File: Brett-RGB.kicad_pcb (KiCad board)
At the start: 2 copper layers, 223 x 71 mm, 182 parts, among them P1 CONN_02X05, P2 USB_OTG, SW1 SW_PUSH, SW10 SW_PUSH, SW11 SW_PUSH, SW12 SW_PUSH, SW13 SW_PUSH, SW14 SW_PUSH, SW15 SW_PUSH, SW16 SW_PUSH, SW17 SW_PUSH, SW18 SW_PUSH, SW19 SW_PUSH, SW2 SW_PUSH, SW20 SW_PUSH, SW21 SW_PUSH, SW22 SW_PUSH, SW23 SW_PUSH, SW24 SW_PUSH, SW25 SW_PUSH, SW26 SW_PUSH, SW27 SW_PUSH, SW28 SW_PUSH, SW29 SW_PUSH, SW3 SW_PUSH, SW30 SW_PUSH, SW31 SW_PUSH, SW32 SW_PUSH, SW33 SW_PUSH, SW34 SW_PUSH, SW35 SW_PUSH, SW36 SW_PUSH, SW37 SW_PUSH, SW38 SW_PUSH, SW39 SW_PUSH, SW4 SW_PUSH, SW40 SW_PUSH, SW41 SW_PUSH, SW42 SW_PUSH, SW43 SW_PUSH, SW44 SW_PUSH, SW45 SW_PUSH, SW46 SW_PUSH, SW47 SW_PUSH, SW48 Reset, SW5 SW_PUSH, SW6 SW_PUSH, SW7 SW_PUSH, SW8 SW_PUSH, SW9 SW_PUSH, U1 IS31FL3732, U2 MK20DX256VLH7, X1 CRYSTAL_SMD

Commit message: Reworked the Board
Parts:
- removed C14, C15, C17, C20, C21: 0.1uF, Capacitors_SMD:C_0603
- removed C18, C19: 1uF, Capacitors_SMD:C_0603
- removed D48: LED, LEDs:LED_0805
- removed D49, D50, D51, D52, D53, D54, D55, D56, D57, D58, D59, D60, D61, D62, D63, D64, D65, D66, D67, D68, D69, D70, D71, D72, D73, D74, D75, D76, D77, D78, D79, D80, D81, D82, D83, D84, D85, D86, D87, D88, D89, D90, D91, D92, D93, D94, D95: D_Small, Diodes_SMD:SOD-123
- added C11: 0.1uF, Capacitors_SMD:C_0603, B.Cu at (97.2, 64.8)
- added LED1: Led_RGB_CA, lib.pretty:RGB-0606, F.Cu at (45.0, 42.0)
- added LED10: Led_RGB_CA, lib.pretty:RGB-0606, F.Cu at (216.0, 42.0)
- added LED11: Led_RGB_CA, lib.pretty:RGB-0606, F.Cu at (235.0, 42.0)
- added LED12: Led_RGB_CA, lib.pretty:RGB-0606, F.Cu at (254.0, 42.0)
- added LED13: Led_RGB_CA, lib.pretty:RGB-0606, F.Cu at (45.0, 61.0)
- added LED14: Led_RGB_CA, lib.pretty:RGB-0606, F.Cu at (64.0, 61.0)
- added LED15: Led_RGB_CA, lib.pretty:RGB-0606, F.Cu at (83.0, 61.0)
- added LED16: Led_RGB_CA, lib.pretty:RGB-0606, F.Cu at (102.0, 61.0)
- added LED17: Led_RGB_CA, lib.pretty:RGB-0606, F.Cu at (121.0, 61.0)
- added LED18: Led_RGB_CA, lib.pretty:RGB-0606, F.Cu at (140.0, 61.0)
- added LED19: Led_RGB_CA, lib.pretty:RGB-0606, F.Cu at (159.0, 61.0)
- added LED2: Led_RGB_CA, lib.pretty:RGB-0606, F.Cu at (64.0, 42.0)
- added LED20: Led_RGB_CA, lib.pretty:RGB-0606, F.Cu at (178.0, 61.0)
- added LED21: Led_RGB_CA, lib.pretty:RGB-0606, F.Cu at (197.0, 61.0)
- added LED22: Led_RGB_CA, lib.pretty:RGB-0606, F.Cu at (216.0, 61.0)
- added LED23: Led_RGB_CA, lib.pretty:RGB-0606, F.Cu at (235.0, 61.0)
- added LED24: Led_RGB_CA, lib.pretty:RGB-0606, F.Cu at (254.0, 61.0)
- added LED25: Led_RGB_CA, lib.pretty:RGB-0606, F.Cu at (45.0, 80.0)
- added LED26: Led_RGB_CA, lib.pretty:RGB-0606, F.Cu at (64.0, 80.0)
- added LED27: Led_RGB_CA, lib.pretty:RGB-0606, F.Cu at (83.0, 80.0)
- added LED28: Led_RGB_CA, lib.pretty:RGB-0606, F.Cu at (102.0, 80.0)
- added LED29: Led_RGB_CA, lib.pretty:RGB-0606, F.Cu at (121.0, 80.0)
- added LED3: Led_RGB_CA, lib.pretty:RGB-0606, F.Cu at (83.0, 42.0)
- added LED30: Led_RGB_CA, lib.pretty:RGB-0606, F.Cu at (140.0, 80.0)
- added LED31: Led_RGB_CA, lib.pretty:RGB-0606, F.Cu at (159.0, 80.0)
- added LED32: Led_RGB_CA, lib.pretty:RGB-0606, F.Cu at (178.0, 80.0)
- added LED33: Led_RGB_CA, lib.pretty:RGB-0606, F.Cu at (197.0, 80.0)
- added LED34: Led_RGB_CA, lib.pretty:RGB-0606, F.Cu at (216.0, 80.0)
- added LED35: Led_RGB_CA, lib.pretty:RGB-0606, F.Cu at (235.0, 80.0)
- added LED36: Led_RGB_CA, lib.pretty:RGB-0606, F.Cu at (254.0, 80.0)
- added LED37: Led_RGB_CA, lib.pretty:RGB-0606, F.Cu at (45.0, 99.0)
- added LED38: Led_RGB_CA, lib.pretty:RGB-0606, F.Cu at (64.0, 99.0)
- added LED39: Led_RGB_CA, lib.pretty:RGB-0606, F.Cu at (83.0, 99.0)
- added LED4: Led_RGB_CA, lib.pretty:RGB-0606, F.Cu at (102.0, 42.0)
- added LED40: Led_RGB_CA, lib.pretty:RGB-0606, F.Cu at (102.0, 99.0)
- added LED41: Led_RGB_CA, lib.pretty:RGB-0606, F.Cu at (121.0, 99.0)
- added LED42: Led_RGB_CA, lib.pretty:RGB-0606, F.Cu at (149.5, 99.0)
- added LED43: Led_RGB_CA, lib.pretty:RGB-0606, F.Cu at (178.0, 99.0)
- added LED44: Led_RGB_CA, lib.pretty:RGB-0606, F.Cu at (197.0, 99.0)
- added LED45: Led_RGB_CA, lib.pretty:RGB-0606, F.Cu at (216.0, 99.0)
- added LED46: Led_RGB_CA, lib.pretty:RGB-0606, F.Cu at (235.0, 99.0)
- added LED47: Led_RGB_CA, lib.pretty:RGB-0606, F.Cu at (254.0, 99.0)
- added LED48: LED, lib.pretty:LED_0805, B.Cu at (87.5, 44.0)
- added LED5: Led_RGB_CA, lib.pretty:RGB-0606, F.Cu at (121.0, 42.0)
- added LED6: Led_RGB_CA, lib.pretty:RGB-0606, F.Cu at (140.0, 42.0)
- added LED7: Led_RGB_CA, lib.pretty:RGB-0606, F.Cu at (159.0, 42.0)
- added LED8: Led_RGB_CA, lib.pretty:RGB-0606, F.Cu at (178.0, 42.0)
- added LED9: Led_RGB_CA, lib.pretty:RGB-0606, F.Cu at (197.0, 42.0)
- added P3: CONN_01X04, lib.pretty:Conn-4, B.Cu at (97.0, 57.0)
- added P4: FLASH_HDR, lib.pretty:JLINK_NEEDLE, B.Cu at (95.0, 51.0)
- added P5: CONN_01X04, lib.pretty:Conn-4, B.Cu at (106.5, 68.8)
- added P6: CONN_01X02, lib.pretty:Conn-2, B.Cu at (92.5, 85.8)
- added P7: CONN_01X02, lib.pretty:Conn-2, B.Cu at (80.5, 75.0)
- added R11: 100, Resistors_SMD:R_0603, B.Cu at (100.0, 59.5)
- C1: value 100uF -> 0.1uF; footprint Capacitors_SMD:C_0805 -> Capacitors_SMD:C_0603
- C12: value 100n -> 0.1uF
- C13, C3: value 1uF -> 0.1uF
- C4: value 0.1uF -> 100uF; footprint Capacitors_SMD:C_0603 -> Capacitors_SMD:C_1206
- C5, C7: value 0.1uF -> 1uF
- C9: value 2.2uF -> 0.1uF
- D1, D10, D11, D12, D13, D14, D15, D16, D17, D18, D19, D2, D20, D21, D22, D23, D24, D25, D26, D27, D28, D29, D3, D30, D31, D32, D33, D34, D35, D36, D37, D38, D39, D4, D40, D41, D42, D43, D44, D45, D46, D47, D5, D6, D7, D8, D9: value LED_RGB -> D_Small; footprint mx2a:plcc-6 -> lib.pretty:SOD-123
- P1: value CONN_02X05 -> USB_OTG; footprint Pin_Headers:Pin_Header_Straight_2x05 -> lib.pretty:Micro-USB_629105150521
- P2: value USB_OTG -> CONN_01X04; footprint Connect:USB_Micro-B -> lib.pretty:Conn-4
- R1: value 1k -> 100k; moved to F.Cu
- R2: moved to F.Cu
- R3: value 33 -> 4.7k; moved to F.Cu
- R4: value 33 -> 100k
- R5: value 5M -> 4.7k; footprint Resistors_SMD:R_0805 -> Resistors_SMD:R_0603; moved to F.Cu
- R6: value 20k -> 33
- R7: value 1k -> 33
- R8: value 1k -> 20k
- R9: value 100k -> 5M; footprint Resistors_SMD:R_0603 -> Resistors_SMD:R_0805
- SW1, SW10, SW11, SW12, SW13, SW14, SW15, SW16, SW17, SW18, SW19, SW2, SW20, SW21, SW22, SW23, SW24, SW25, SW26, SW27, SW28, SW29, SW3, SW30, SW31, SW32, SW33, SW34, SW35, SW36, SW37, SW38, SW39, SW4, SW40, SW41, SW42, SW43, SW44, SW45, SW46, SW47, SW5, SW6, SW7, SW8, SW9: footprint mx2a:RomerG -> lib.pretty:RomerG
- SW48: value Reset -> TAC_SWITCH; footprint mx2a:KSEM31GLFS -> lib.pretty:PTS810
- U1: value IS31FL3732 -> IS31FL3737
- U2: value MK20DX256VLH7 -> MK20DX256VLH7-RESCUE-RainbowFox
- moved C4 66.4 mm to (73.5, 43.5)
- moved R4 50.7 mm to (115.8, 72.0), turned to 180 degrees
- moved R6 42.3 mm to (81.5, 70.0), turned to 180 degrees
- moved R3 42.1 mm to (103.5, 71.2), turned to 90 degrees
- moved P1 39.9 mm to (73.5, 32.0), turned to 0 degrees
- moved R7 39.3 mm to (81.5, 72.0), turned to 180 degrees
- moved R9 38.9 mm to (84.5, 68.2)
- moved P2 34.8 mm to (78.0, 72.0), turned to 90 degrees
- moved R1 28.1 mm to (107.5, 71.2)
- moved C5 28.0 mm to (107.2, 72.8), turned to 90 degrees
- moved C3 26.5 mm to (108.8, 72.8), turned to 90 degrees
- moved C13 25.1 mm to (102.0, 72.8), turned to 0 degrees
- moved C2 24.4 mm to (111.0, 72.2), turned to 180 degrees
- moved C12 22.2 mm to (92.5, 39.5), turned to 90 degrees
- moved C1 20.1 mm to (111.0, 70.8), turned to 180 degrees
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- renumbered REF** to ?
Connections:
- net /MCU/X+ renamed Net-(U2-Pad32)
- net /MCU/X- renamed Net-(U2-Pad33)
- C1 pad 1: GND -> +3V3
- C1 pad 2: +5V -> GND
- C10 pad 1: GND -> +5V
- C10 pad 2: +5V -> GND
- C13 pad 1: +5V -> +3V3
- C2 pad 1: +5V -> +3V3
- C6 pad 1: +3V3 -> +5V
- C7 pad 1: +3V3 -> +5V
- C8 pad 2: GND -> Net-(C8-Pad2)
- C9 pad 1: Net-(C9-Pad1) -> +3V3
- C9 pad 2: +3V3 -> GND
- D1 pad 1: /MCU/A1 -> /MCU/PTD0
- D1 pad 2: /MCU/A2 -> Net-(D1-Pad2)
- D10 pad 1: /MCU/A9 -> /MCU/PTC9
- D10 pad 2: /MCU/A9 -> Net-(D10-Pad2)
- D11 pad 1: /MCU/A7 -> /MCU/PTC9
- D11 pad 2: /MCU/A7 -> Net-(D11-Pad2)
- D12 pad 1: /MCU/A7 -> /MCU/PTC9
- D12 pad 2: /MCU/A8 -> Net-(D12-Pad2)
- D13 pad 1: /MCU/A5 -> /MCU/PTD1
- D13 pad 2: /MCU/A5 -> Net-(D13-Pad2)
- D14 pad 1: /MCU/A4 -> /MCU/PTD1
- D14 pad 2: /MCU/A4 -> Net-(D14-Pad2)
- D15 pad 1: /MCU/A3 -> /MCU/PTD1
- D15 pad 2: /MCU/A2 -> Net-(D15-Pad2)
- D16 pad 1: /MCU/A2 -> /MCU/PTD1
- D16 pad 2: /MCU/A3 -> Net-(D16-Pad2)
- D17 pad 1: /MCU/A1 -> /MCU/PTD1
- D17 pad 2: /MCU/A1 -> Net-(D17-Pad2)
- D18 pad 1: /MCU/A6 -> /MCU/PTD1
- D18 pad 2: /MCU/A6 -> Net-(D18-Pad2)
- D19 pad 1: /MCU/A5 -> /MCU/PTC8
- D19 pad 2: /MCU/A4 -> Net-(D19-Pad2)
- D2 pad 1: /MCU/A3 -> /MCU/PTD0
- D2 pad 2: /MCU/A2 -> Net-(D2-Pad2)
- D20 pad 1: /MCU/A4 -> /MCU/PTC8
- D20 pad 2: /MCU/A4 -> Net-(D20-Pad2)
- D21 pad 1: /MCU/A7 -> /MCU/PTC8
- D21 pad 2: /MCU/A8 -> Net-(D21-Pad2)
- D22 pad 1: /MCU/A5 -> /MCU/PTC8
- D22 pad 2: /MCU/A5 -> Net-(D22-Pad2)
- D23 pad 1: /MCU/A7 -> /MCU/PTC8
- D23 pad 2: /MCU/A8 -> Net-(D23-Pad2)
- D24 pad 1: /MCU/A6 -> /MCU/PTC8
- D24 pad 2: /MCU/A6 -> Net-(D24-Pad2)
- D25 pad 1: /MCU/B7 -> /MCU/PTD4
- D25 pad 2: /MCU/B8 -> Net-(D25-Pad2)
- D26 pad 1: /MCU/B7 -> /MCU/PTD4
- D26 pad 2: /MCU/B8 -> Net-(D26-Pad2)
- D27 pad 1: /MCU/B4 -> /MCU/PTD4
- D27 pad 2: /MCU/B4 -> Net-(D27-Pad2)
- D28 pad 1: /MCU/B5 -> /MCU/PTD4
- D28 pad 2: /MCU/B6 -> Net-(D28-Pad2)
- D29 pad 1: /MCU/B4 -> /MCU/PTD4
- D29 pad 2: /MCU/B4 -> Net-(D29-Pad2)
- D3 pad 1: /MCU/A6 -> /MCU/PTD0
- D3 pad 2: /MCU/A6 -> Net-(D3-Pad2)
- D30 pad 1: /MCU/B3 -> /MCU/PTD4
- D30 pad 2: /MCU/B3 -> Net-(D30-Pad2)
- D31 pad 1: /MCU/B2 -> /MCU/PTC7
- D31 pad 2: /MCU/B1 -> Net-(D31-Pad2)
- D32 pad 1: /MCU/B1 -> /MCU/PTC7
- D32 pad 2: /MCU/B2 -> Net-(D32-Pad2)
- D33 pad 1: /MCU/B4 -> /MCU/PTC7
- D33 pad 2: /MCU/B4 -> Net-(D33-Pad2)
- D34 pad 1: /MCU/B1 -> /MCU/PTC7
- D34 pad 2: /MCU/B2 -> Net-(D34-Pad2)
- D35 pad 1: /MCU/B5 -> /MCU/PTC7
- D35 pad 2: /MCU/B5 -> Net-(D35-Pad2)
- D36 pad 1: /MCU/B1 -> /MCU/PTC7
- D36 pad 2: /MCU/B2 -> Net-(D36-Pad2)
- D37 pad 1: /MCU/B5 -> /MCU/PTC11
- D37 pad 2: /MCU/B5 -> Net-(D37-Pad2)
- D38 pad 1: /MCU/B9 -> /MCU/PTC11
- D38 pad 2: /MCU/B9 -> Net-(D38-Pad2)
- D39 pad 1: /MCU/B8 -> /MCU/PTC11
- D39 pad 2: /MCU/B7 -> Net-(D39-Pad2)
- D4 pad 1: /MCU/A3 -> /MCU/PTD0
- D4 pad 2: /MCU/A2 -> Net-(D4-Pad2)
- D40 pad 1: /MCU/B6 -> /MCU/PTC11
- D40 pad 2: /MCU/B6 -> Net-(D40-Pad2)
- D41 pad 1: /MCU/B9 -> /MCU/PTC11
- D41 pad 2: /MCU/B8 -> Net-(D41-Pad2)
- D42 pad 1: /MCU/B9 -> /MCU/PTC11
- D42 pad 2: /MCU/B9 -> Net-(D42-Pad2)
- D43 pad 1: /MCU/B3 -> /MCU/PTC10
- D43 pad 2: /MCU/B2 -> Net-(D43-Pad2)
- D44 pad 1: /MCU/B1 -> /MCU/PTC10
- D44 pad 2: /MCU/B2 -> Net-(D44-Pad2)
- D45 pad 1: /MCU/B7 -> /MCU/PTC10
- D45 pad 2: /MCU/B7 -> Net-(D45-Pad2)
- D46 pad 1: /MCU/B1 -> /MCU/PTC10
- D46 pad 2: /MCU/B2 -> Net-(D46-Pad2)
- D47 pad 1: /MCU/B6 -> /MCU/PTC10
- D47 pad 2: /MCU/B6 -> Net-(D47-Pad2)
- D5 pad 1: /MCU/A7 -> /MCU/PTD0
- D5 pad 2: /MCU/A7 -> Net-(D5-Pad2)
- D6 pad 1: /MCU/A3 -> /MCU/PTD0
- D6 pad 2: /MCU/A2 -> Net-(D6-Pad2)
- D7 pad 1: /MCU/A8 -> /MCU/PTC9
- D7 pad 2: /MCU/A8 -> Net-(D7-Pad2)
- D8 pad 1: /MCU/A3 -> /MCU/PTC9
- D8 pad 2: /MCU/A2 -> Net-(D8-Pad2)
- D9 pad 1: /MCU/A9 -> /MCU/PTC9
- D9 pad 2: /MCU/A9 -> Net-(D9-Pad2)
- P1 pad 1: GND -> +5V
- P1 pad 2: (no net) -> /MCU/USB_D-
- P1 pad 3: +5V -> /MCU/USB_D+
- P1 pad 5: (no net) -> GND
- P2 pad 2: Net-(P2-Pad2) -> /MCU/USB_D-
- P2 pad 3: Net-(P2-Pad3) -> /MCU/USB_D+
- P2 pad 4: (no net) -> GND
- R1 pad 1: Net-(D48-Pad1) -> GND
- R1 pad 2: GND -> /MCU/SDB
- R10 pad 1: /MCU/SWD_CLK -> Net-(R10-Pad1)
- R10 pad 2: Net-(R10-Pad2) -> /MCU/SWD_CLK
- R2 pad 1: /MCU/INTB -> +3V3
- R2 pad 2: Net-(R2-Pad2) -> /MCU/INTB
- R3 pad 1: Net-(P2-Pad2) -> +3V3
- R3 pad 2: /MCU/D- -> /MCU/SCL
- R4 pad 1: Net-(P2-Pad3) -> GND
- R4 pad 2: /MCU/D+ -> Net-(R4-Pad2)
- R5 pad 1: Net-(C9-Pad1) -> +3V3
- R5 pad 2: GND -> /MCU/SDA
- R6 pad 1: GND -> /MCU/D-
- R6 pad 2: /MCU/R_Ext -> /MCU/USB_D-
- R7 pad 1: /MCU/SCL -> /MCU/D+
- R7 pad 2: +3V3 -> /MCU/USB_D+
- R8 pad 1: /MCU/SDA -> Net-(R8-Pad1)
- R8 pad 2: +3V3 -> GND
- R9 pad 1: GND -> Net-(C8-Pad2)
- R9 pad 2: /MCU/SDB -> GND
- SW1 pad 1: Net-(D49-Pad2) -> Net-(D1-Pad2)
- SW1 pad 2: /MCU/Col1 -> /MCU/PTD7
- SW10 pad 1: Net-(D58-Pad2) -> Net-(D10-Pad2)
- SW10 pad 2: /MCU/Col3 -> /MCU/PTD5
- SW11 pad 1: Net-(D59-Pad2) -> Net-(D11-Pad2)
- SW11 pad 2: /MCU/Col2 -> /MCU/PTD6
- SW12 pad 1: Net-(D60-Pad2) -> Net-(D12-Pad2)
- SW12 pad 2: /MCU/Col1 -> /MCU/PTD7
- SW13 pad 1: Net-(D61-Pad2) -> Net-(D13-Pad2)
- SW13 pad 2: /MCU/Col1 -> /MCU/PTD7
- SW14 pad 1: Net-(D62-Pad2) -> Net-(D14-Pad2)
- SW14 pad 2: /MCU/Col2 -> /MCU/PTD6
- SW15 pad 1: Net-(D63-Pad2) -> Net-(D15-Pad2)
- SW15 pad 2: /MCU/Col3 -> /MCU/PTD5
- SW16 pad 1: Net-(D64-Pad2) -> Net-(D16-Pad2)
- SW16 pad 2: /MCU/Col4 -> /MCU/PTB18
- SW17 pad 1: Net-(D65-Pad2) -> Net-(D17-Pad2)
- SW17 pad 2: /MCU/Col5 -> /MCU/PTB2
- SW18 pad 1: Net-(D66-Pad2) -> Net-(D18-Pad2)
- SW18 pad 2: /MCU/Col6 -> /MCU/PTB3
- SW19 pad 1: Net-(D67-Pad2) -> Net-(D19-Pad2)
- SW19 pad 2: /MCU/Col6 -> /MCU/PTB3
- SW2 pad 1: Net-(D50-Pad2) -> Net-(D2-Pad2)
- SW2 pad 2: /MCU/Col2 -> /MCU/PTD6
- SW20 pad 1: Net-(D68-Pad2) -> Net-(D20-Pad2)
- SW20 pad 2: /MCU/Col5 -> /MCU/PTB2
- SW21 pad 1: Net-(D69-Pad2) -> Net-(D21-Pad2)
- SW21 pad 2: /MCU/Col4 -> /MCU/PTB18
- SW22 pad 1: Net-(D70-Pad2) -> Net-(D22-Pad2)
- SW22 pad 2: /MCU/Col3 -> /MCU/PTD5
- SW23 pad 1: Net-(D71-Pad2) -> Net-(D23-Pad2)
- SW23 pad 2: /MCU/Col2 -> /MCU/PTD6
- SW24 pad 1: Net-(D72-Pad2) -> Net-(D24-Pad2)
- SW24 pad 2: /MCU/Col1 -> /MCU/PTD7
- SW25 pad 1: Net-(D73-Pad2) -> Net-(D25-Pad2)
- SW25 pad 2: /MCU/Col1 -> /MCU/PTD7
- SW26 pad 1: Net-(D74-Pad2) -> Net-(D26-Pad2)
- SW26 pad 2: /MCU/Col2 -> /MCU/PTD6
- SW27 pad 1: Net-(D75-Pad2) -> Net-(D27-Pad2)
- SW27 pad 2: /MCU/Col3 -> /MCU/PTD5
- SW28 pad 1: Net-(D76-Pad2) -> Net-(D28-Pad2)
- SW28 pad 2: /MCU/Col4 -> /MCU/PTB18
- SW29 pad 1: Net-(D77-Pad2) -> Net-(D29-Pad2)
- SW29 pad 2: /MCU/Col5 -> /MCU/PTB2
- SW3 pad 1: Net-(D51-Pad2) -> Net-(D3-Pad2)
- SW3 pad 2: /MCU/Col3 -> /MCU/PTD5
- SW30 pad 1: Net-(D78-Pad2) -> Net-(D30-Pad2)
- SW30 pad 2: /MCU/Col6 -> /MCU/PTB3
- SW31 pad 1: Net-(D79-Pad2) -> Net-(D31-Pad2)
- SW31 pad 2: /MCU/Col6 -> /MCU/PTB3
- SW32 pad 1: Net-(D80-Pad2) -> Net-(D32-Pad2)
- SW32 pad 2: /MCU/Col5 -> /MCU/PTB2
- SW33 pad 1: Net-(D81-Pad2) -> Net-(D33-Pad2)
- SW33 pad 2: /MCU/Col4 -> /MCU/PTB18
- SW34 pad 1: Net-(D82-Pad2) -> Net-(D34-Pad2)
- SW34 pad 2: /MCU/Col3 -> /MCU/PTD5
- SW35 pad 1: Net-(D83-Pad2) -> Net-(D35-Pad2)
- SW35 pad 2: /MCU/Col2 -> /MCU/PTD6
- SW36 pad 1: Net-(D84-Pad2) -> Net-(D36-Pad2)
- SW36 pad 2: /MCU/Col1 -> /MCU/PTD7
- SW37 pad 1: Net-(D85-Pad2) -> Net-(D37-Pad2)
- SW37 pad 2: /MCU/Col1 -> /MCU/PTD7
- SW38 pad 1: Net-(D86-Pad2) -> Net-(D38-Pad2)
- SW38 pad 2: /MCU/Col2 -> /MCU/PTD6
- SW39 pad 1: Net-(D87-Pad2) -> Net-(D39-Pad2)
- SW39 pad 2: /MCU/Col3 -> /MCU/PTD5
- SW4 pad 1: Net-(D52-Pad2) -> Net-(D4-Pad2)
- SW4 pad 2: /MCU/Col4 -> /MCU/PTB18
- SW40 pad 1: Net-(D88-Pad2) -> Net-(D40-Pad2)
- SW40 pad 2: /MCU/Col4 -> /MCU/PTB18
- SW41 pad 1: Net-(D89-Pad2) -> Net-(D41-Pad2)
- SW41 pad 2: /MCU/Col5 -> /MCU/PTB2
- SW42 pad 1: Net-(D90-Pad2) -> Net-(D42-Pad2)
- SW42 pad 2: /MCU/Col6 -> /MCU/PTB3
- SW43 pad 1: Net-(D91-Pad2) -> Net-(D43-Pad2)
- SW43 pad 2: /MCU/Col5 -> /MCU/PTB2
- SW44 pad 1: Net-(D92-Pad2) -> Net-(D44-Pad2)
- SW44 pad 2: /MCU/Col4 -> /MCU/PTB18
- SW45 pad 1: Net-(D93-Pad2) -> Net-(D45-Pad2)
- SW45 pad 2: /MCU/Col3 -> /MCU/PTD5
- SW46 pad 1: Net-(D94-Pad2) -> Net-(D46-Pad2)
- SW46 pad 2: /MCU/Col2 -> /MCU/PTD6
- SW47 pad 1: Net-(D95-Pad2) -> Net-(D47-Pad2)
- SW47 pad 2: /MCU/Col1 -> /MCU/PTD7
- SW48 pad 1: /MCU/MCU_RESET -> (no net)
- SW48 pad 2: GND -> /MCU/MCU_RESET
- SW48 pad 4: (no net) -> GND
- SW5 pad 1: Net-(D53-Pad2) -> Net-(D5-Pad2)
- SW5 pad 2: /MCU/Col5 -> /MCU/PTB2
- SW6 pad 1: Net-(D54-Pad2) -> Net-(D6-Pad2)
- SW6 pad 2: /MCU/Col6 -> /MCU/PTB3
- SW7 pad 1: Net-(D55-Pad2) -> Net-(D7-Pad2)
- SW7 pad 2: /MCU/Col6 -> /MCU/PTB3
- SW8 pad 1: Net-(D56-Pad2) -> Net-(D8-Pad2)
- SW8 pad 2: /MCU/Col5 -> /MCU/PTB2
- SW9 pad 1: Net-(D57-Pad2) -> Net-(D9-Pad2)
- SW9 pad 2: /MCU/Col4 -> /MCU/PTB18
- U1 pad 1: +5V -> /MCU/SW1
- U1 pad 10: (no net) -> /MCU/SW9
- U1 pad 11: /MCU/B1 -> GND
- U1 pad 12: /MCU/B2 -> /MCU/SW10
- U1 pad 13: /MCU/B3 -> /MCU/SW11
- U1 pad 14: /MCU/B4 -> /MCU/SW12
- U1 pad 15: /MCU/B5 -> /MCU/CS1
- U1 pad 16: /MCU/B6 -> /MCU/CS2
- U1 pad 17: /MCU/B7 -> /MCU/CS3
- U1 pad 18: /MCU/B8 -> /MCU/CS4
- U1 pad 19: /MCU/B9 -> +5V
- U1 pad 2: (no net) -> /MCU/SW2
- U1 pad 20: +5V -> /MCU/CS5
- U1 pad 21: /MCU/SDA -> /MCU/CS6
- U1 pad 22: /MCU/SCL -> /MCU/CS7
- U1 pad 23: GND -> /MCU/CS8
- U1 pad 24: GND -> /MCU/CS9
- U1 pad 25: /MCU/SDB -> /MCU/CS10
- U1 pad 27: +3V3 -> /MCU/CS11
- U1 pad 28: /MCU/R_Ext -> /MCU/CS12
- U1 pad 29: /MCU/C_Filt -> GND
- U1 pad 3: (no net) -> /MCU/SW3
- U1 pad 30: (no net) -> Net-(R8-Pad1)
- U1 pad 31: GND -> +5V
- U1 pad 32: /MCU/A1 -> +3V3
- U1 pad 33: /MCU/A2 -> (no net)
- U1 pad 34: /MCU/A3 -> /MCU/SDA
- U1 pad 35: /MCU/A4 -> /MCU/SCL
- U1 pad 36: /MCU/A5 -> GND
- U1 pad 37: /MCU/A6 -> /MCU/INTB
- U1 pad 38: /MCU/A7 -> /MCU/SDB
- U1 pad 39: /MCU/A8 -> Net-(R4-Pad2)
- U1 pad 4: +5V -> GND
- U1 pad 40: /MCU/A9 -> GND
- U1 pad 5: Net-(R2-Pad2) -> /MCU/SW4
- U1 pad 6: (no net) -> /MCU/SW5
- U1 pad 7: GND -> /MCU/SW6
- U1 pad 8: GND -> /MCU/SW7
- U1 pad 9: GND -> /MCU/SW8
- U2 pad 1: /MCU/Col2 -> /MCU/RX1
- U2 pad 2: /MCU/Col1 -> /MCU/TX1
- U2 pad 22: Net-(R10-Pad2) -> Net-(R10-Pad1)
- U2 pad 25: (no net) -> Net-(R11-Pad1)
- U2 pad 26: /MCU/Row1 -> (no net)
- U2 pad 28: /MCU/Row2 -> (no net)
- U2 pad 29: /MCU/Row5 -> (no net)
- U2 pad 37: /MCU/SDB -> /MCU/PTB2
- U2 pad 38: /MCU/INTB -> /MCU/PTB3
- U2 pad 39: (no net) -> /MCU/SDB
- U2 pad 40: (no net) -> /MCU/INTB
- U2 pad 41: (no net) -> /MCU/PTB18
- U2 pad 49: /MCU/Row8 -> (no net)
- U2 pad 50: /MCU/Col5 -> (no net)
- U2 pad 51: /MCU/Col6 -> (no net)
- U2 pad 52: (no net) -> /MCU/PTC7
- U2 pad 53: (no net) -> /MCU/PTC8
- U2 pad 54: (no net) -> /MCU/PTC9
- U2 pad 55: (no net) -> /MCU/PTC10
- U2 pad 56: /MCU/Row7 -> /MCU/PTC11
- U2 pad 57: /MCU/Row6 -> /MCU/PTD0
- U2 pad 58: (no net) -> /MCU/PTD1
- U2 pad 59: (no net) -> /MCU/RX2
- U2 pad 60: (no net) -> /MCU/TX2
- U2 pad 61: /MCU/Row4 -> /MCU/PTD4
- U2 pad 62: /MCU/Row3 -> /MCU/PTD5
- U2 pad 63: /MCU/Col3 -> /MCU/PTD6
- U2 pad 64: /MCU/Col4 -> /MCU/PTD7
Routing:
- net /MCU/Col1: track 389.3 -> 0.00 mm
- net /MCU/PTD5: track 0.00 -> 388.2 mm
- net /MCU/PTD7: track 0.00 -> 382.2 mm, vias 0 -> 1
- net /MCU/PTD6: track 0.00 -> 327.4 mm
- net /MCU/Col2: track 326.1 -> 0.00 mm, vias 1 -> 0
- net /MCU/PTB18: track 0.00 -> 319.1 mm, vias 0 -> 3
- net /MCU/B7: track 314.2 -> 0.00 mm, vias 1 -> 0
- net /MCU/A7: track 312.9 -> 0.00 mm, vias 1 -> 0
- net /MCU/PTC9: track 0.00 -> 311.0 mm, vias 0 -> 1
- net /MCU/A2: track 306.7 -> 0.00 mm, vias 1 -> 0
- net /MCU/A1: track 301.2 -> 0.00 mm, vias 1 -> 0
- net /MCU/B5: track 299.7 -> 0.00 mm, vias 3 -> 0
- net /MCU/B2: track 299.3 -> 0.00 mm, vias 1 -> 0
- net /MCU/A3: track 294.2 -> 0.00 mm, vias 1 -> 0
- net /MCU/B1: track 293.3 -> 0.00 mm, vias 1 -> 0
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- removed copper zone on B.Cu, net +5V
- removed copper zone on F.Cu, net +5V
- removed copper zone on B.Cu, net GND
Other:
- board size 223 x 71 mm -> 223 x 73.5 mm
- net class Default: via_dia 0.6 -> 0.65

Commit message: Added Fiducials and Pintout Description
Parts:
- added ?: , Fiducials:Fiducial_1mm_Dia_2.54mm_Outer_CopperTop, F.Cu at (98.0, 89.5)
- added ?: , Fiducials:Fiducial_1mm_Dia_2.54mm_Outer_CopperBottom, F.Cu at (225.5, 51.5)
- added ?: , Fiducials:Fiducial_1mm_Dia_2.54mm_Outer_CopperTop, F.Cu at (66.0, 52.0)
- added ?: , Fiducials:Fiducial_1mm_Dia_2.54mm_Outer_CopperBottom, F.Cu at (66.0, 52.0)
- added ?: , Fiducials:Fiducial_1mm_Dia_2.54mm_Outer_CopperBottom, F.Cu at (98.0, 89.5)
- added ?: , Fiducials:Fiducial_1mm_Dia_2.54mm_Outer_CopperBottom, F.Cu at (72.0, 73.0)
- added ?: , Fiducials:Fiducial_1mm_Dia_2.54mm_Outer_CopperTop, F.Cu at (72.0, 73.0)
- added ?: , Fiducials:Fiducial_1mm_Dia_2.54mm_Outer_CopperTop, F.Cu at (111.0, 51.5)
- added ?: , Fiducials:Fiducial_1mm_Dia_2.54mm_Outer_CopperBottom, F.Cu at (111.0, 51.5)
- added ?: , Fiducials:Fiducial_1mm_Dia_2.54mm_Outer_CopperBottom, F.Cu at (225.5, 90.5)
- added ?: , Fiducials:Fiducial_1mm_Dia_2.54mm_Outer_CopperTop, F.Cu at (225.5, 90.5)
- added ?: , Fiducials:Fiducial_1mm_Dia_2.54mm_Outer_CopperTop, F.Cu at (225.5, 51.5)
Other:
- board text added: "5V"
- board text added: "D+"
- board text added: "D-"
- board text added: "GND"
- board text added: "INTB"
- board text added: "RX1"
- board text added: "RX2"
- board text added: "SCL"
- board text added: "SDA"
- board text added: "SDB"
- board text added: "SWD_CLK"
- board text added: "SWD_DIO"
- board text added: "TX1"
- board text added: "TX2"

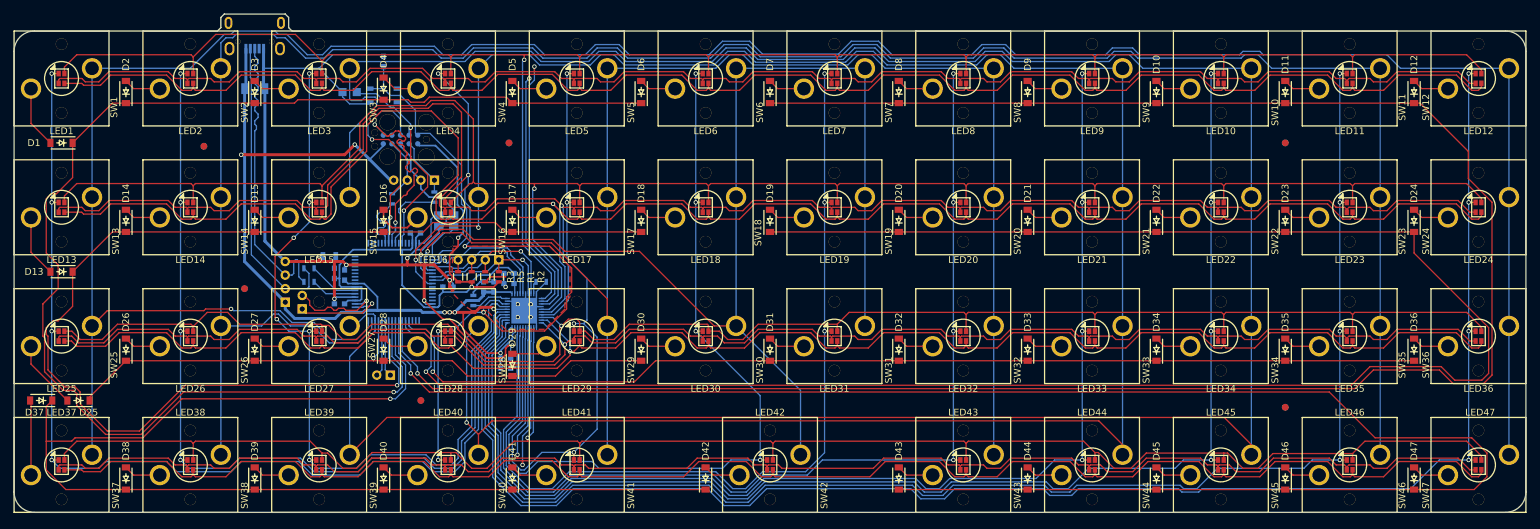
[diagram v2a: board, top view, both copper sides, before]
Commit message: Performed the changes from https://github.com/Project-Aurora/RainbowFox/commit/d956c5c3914152606eb0eeb9caeb00dc6e36fd84
Added Resistor to ground for firmware-LED
Connect VBAT to 3.3V
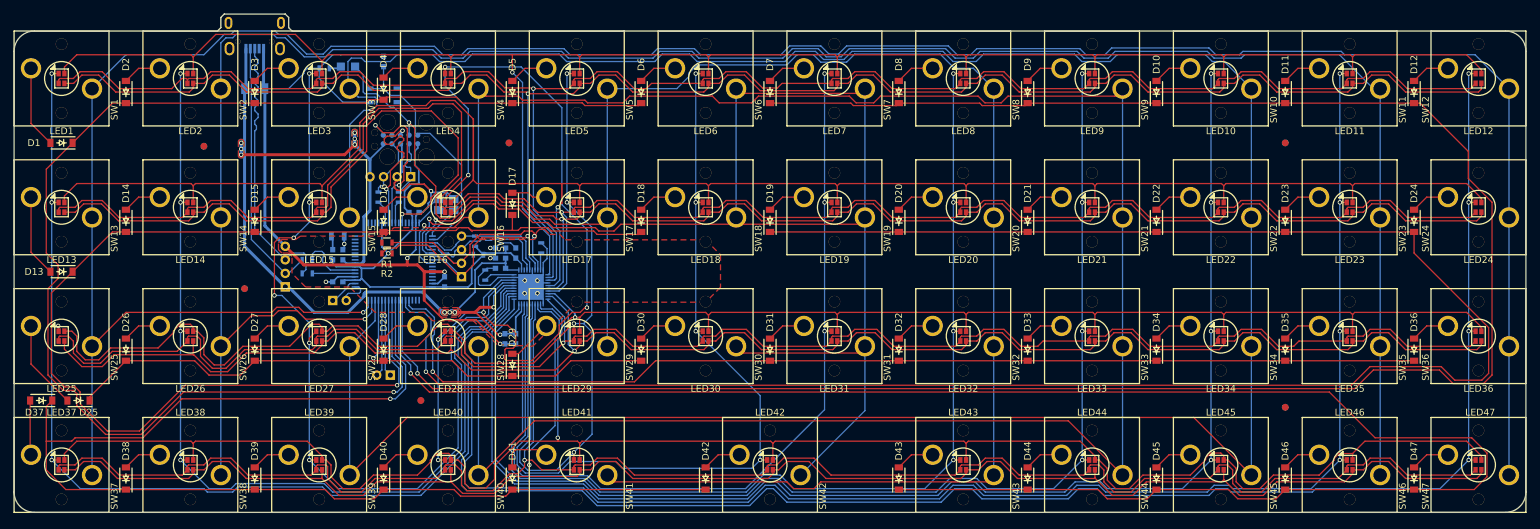
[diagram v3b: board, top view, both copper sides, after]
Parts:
- added R12: 1k, Resistors_SMD:R_0603, B.Cu at (83.8, 40.5)
- R3, R5: moved to B.Cu
- moved R2 16.9 mm to (93.0, 67.8), turned to 180 degrees
- moved R1 15.4 mm to (93.0, 66.2), turned to 0 degrees
- moved R3 5.81 mm to (106.0, 66.0)
- moved P7 5.51 mm to (86.0, 74.8), turned to 0 degrees
- moved C2 5.40 mm to (109.8, 67.0)
- moved R11 5.25 mm to (94.8, 59.5)
- moved R4 5.00 mm to (115.8, 67.0), turned to 270 degrees
- moved C5 4.93 mm to (109.8, 68.5), turned to 180 degrees
- moved C7 4.35 mm to (110.4, 80.4), turned to 270 degrees
- moved R8 4.14 mm to (107.5, 71.0)
- moved LED48 3.76 mm to (87.2, 40.2)
- moved U1 3.64 mm to (114.2, 72.8)
- moved P3 3.54 mm to (93.5, 56.5)
- moved R5 3.40 mm to (106.5, 68.0), turned to 180 degrees
- moved C9 3.26 mm to (85.8, 72.0)
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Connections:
- net /MCU/CS1 renamed /CS1
- net /MCU/CS10 renamed /CS10
- net /MCU/CS11 renamed /CS11
- net /MCU/CS12 renamed /CS12
- net /MCU/CS2 renamed /CS2
- net /MCU/CS3 renamed /CS3
- net /MCU/CS4 renamed /CS4
- net /MCU/CS5 renamed /CS5
- net /MCU/CS6 renamed /CS6
- net /MCU/CS7 renamed /CS7
- net /MCU/CS8 renamed /CS8
- net /MCU/CS9 renamed /CS9
- net /MCU/PTB18 renamed /Col4
- net /MCU/PTB2 renamed /Col5
- net /MCU/PTB3 renamed /Col6
- net /MCU/PTC10 renamed /Row8
- net /MCU/PTC11 renamed /Row4
- net /MCU/PTC7 renamed /Row7
- net /MCU/PTC8 renamed /Row6
- net /MCU/PTC9 renamed /Row5
- net /MCU/PTD0 renamed /Row1
- net /MCU/PTD1 renamed /Row2
- net /MCU/PTD4 renamed /Row3
- net /MCU/PTD5 renamed /Col3
- net /MCU/PTD6 renamed /Col2
- net /MCU/PTD7 renamed /Col1
- net /MCU/SW1 renamed /SW1
- net /MCU/SW10 renamed /SW10
- net /MCU/SW11 renamed /SW11
- net /MCU/SW12 renamed /SW12
- net /MCU/SW2 renamed /SW2
- net /MCU/SW3 renamed /SW3
- net /MCU/SW4 renamed /SW4
- net /MCU/SW5 renamed /SW5
- net /MCU/SW6 renamed /SW6
- net /MCU/SW7 renamed /SW7
- net /MCU/SW8 renamed /SW8
- net /MCU/SW9 renamed /SW9
- LED48 pad 1: GND -> Net-(LED48-Pad1)
- P7 pad 1: /MCU/RX1 -> /MCU/TX1
- P7 pad 2: /MCU/TX1 -> /MCU/RX1
- U2 pad 21: (no net) -> +3V3
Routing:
- net /Col5: track 213.5 -> 250.4 mm
- net /CS12: track 106.5 -> 138.5 mm
- net +3V3: track 90.5 -> 71.5 mm, vias 2 -> 1
- net /Col6: track 176.3 -> 195.3 mm
- net /SW10: track 255.8 -> 274.7 mm
- net /MCU/INTB: track 21.6 -> 39.3 mm
- net /SW12: track 250.1 -> 267.7 mm
- net +5V: track 140.1 -> 154.4 mm, vias 7 -> 11
- net /MCU/SDB: track 23.4 -> 35.8 mm
- net /SW9: track 239.8 -> 252.0 mm
- net /SW7: track 246.2 -> 258.1 mm
- net /SW2: track 277.1 -> 265.4 mm
- net /CS7: track 219.6 -> 231.1 mm
- net /SW5: track 286.0 -> 274.5 mm
- net /CS8: track 240.5 -> 251.9 mm
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- added copper zone on B.Cu, net +5V
- added copper zone on F.Cu, net +5V

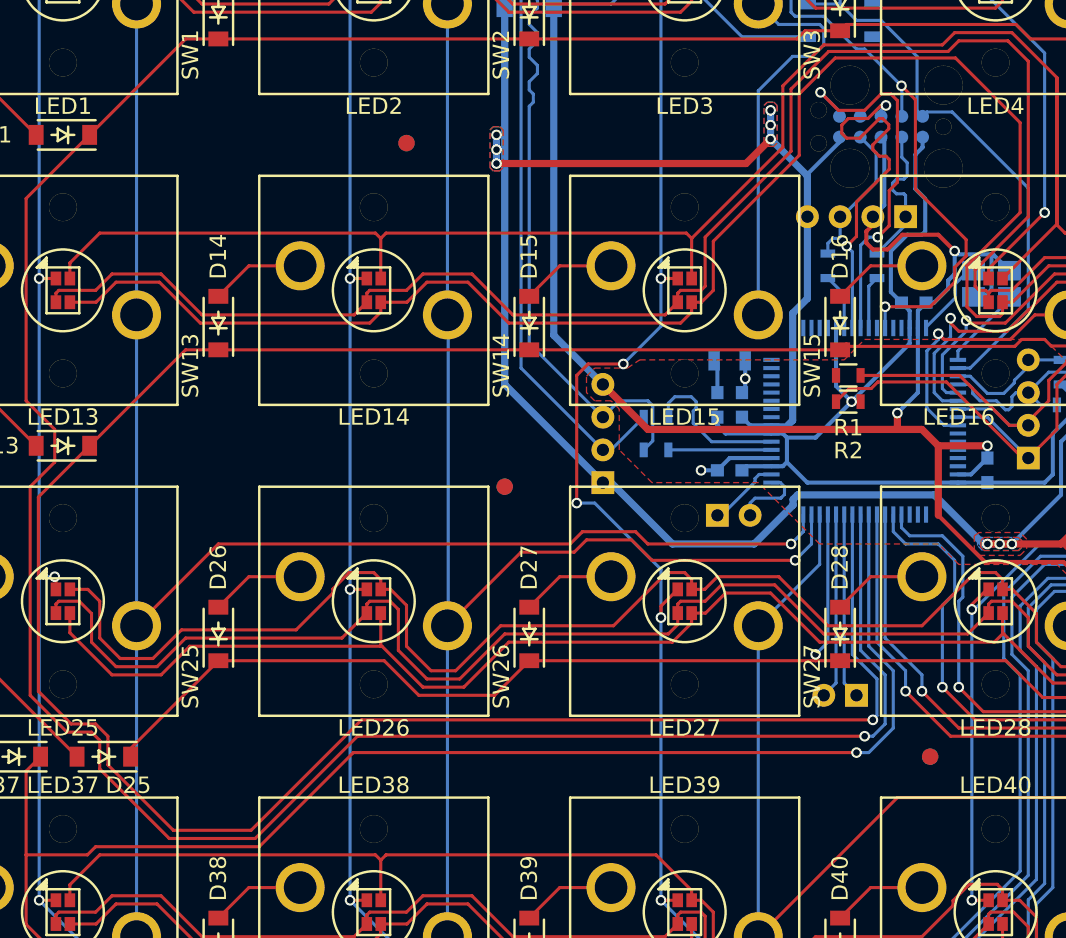
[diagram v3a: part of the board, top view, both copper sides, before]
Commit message: Added Pinout for 3.3V
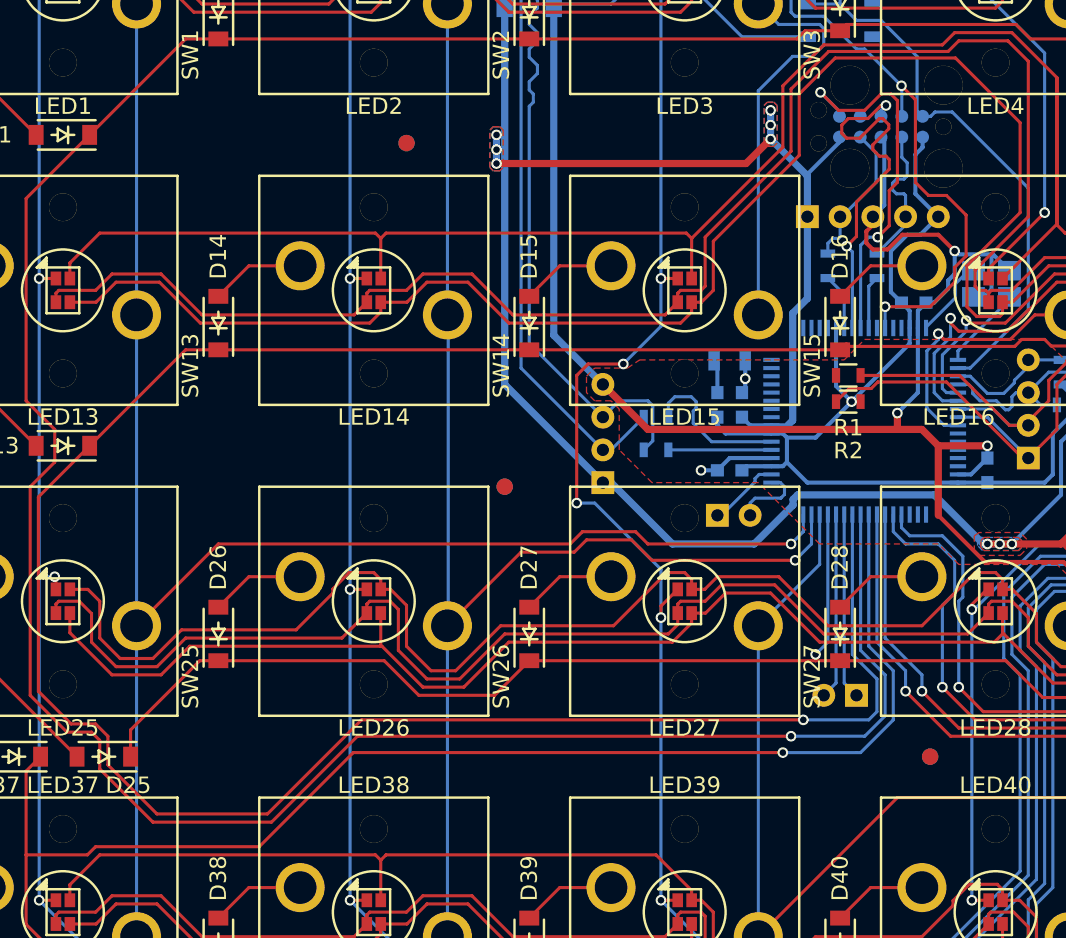
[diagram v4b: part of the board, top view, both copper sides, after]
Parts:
- P3: value CONN_01X04 -> CONN_01X05; footprint lib.pretty:Conn-4 -> lib.pretty:Conn-5
- moved P3 1.00 mm to (94.5, 56.5), turned to 0 degrees
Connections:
- P3 pad 1: /MCU/SWD_DIO -> +5V
- P3 pad 2: GND -> /MCU/SWD_CLK
- P3 pad 3: /MCU/SWD_CLK -> GND
- P3 pad 4: +5V -> /MCU/SWD_DIO
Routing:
- net /Row3: track 97.2 -> 98.4 mm
- net /Row1: track 197.9 -> 196.8 mm
- net /Row2: track 178.9 -> 177.9 mm
- net /MCU/PTA5: track 34.9 -> 35.5 mm
- net +3V3: track 71.5 -> 72.1 mm
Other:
- board text added: "3.3V"
